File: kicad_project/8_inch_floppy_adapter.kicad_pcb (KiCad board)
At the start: 2 copper layers, 100 x 50 mm, 13 parts, among them J1 IDC02x17, J2 IDC02x17, J3 IDC02x25

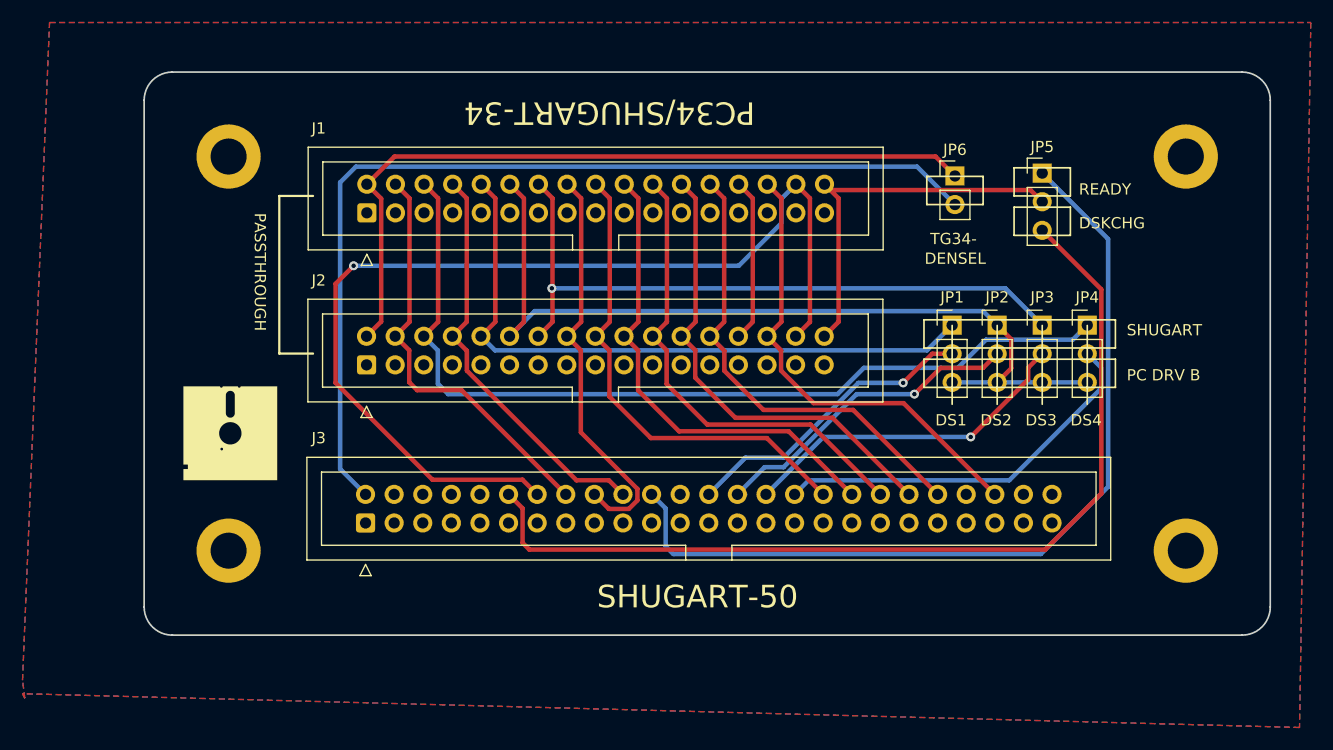
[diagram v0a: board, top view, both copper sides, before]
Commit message: Refine routing
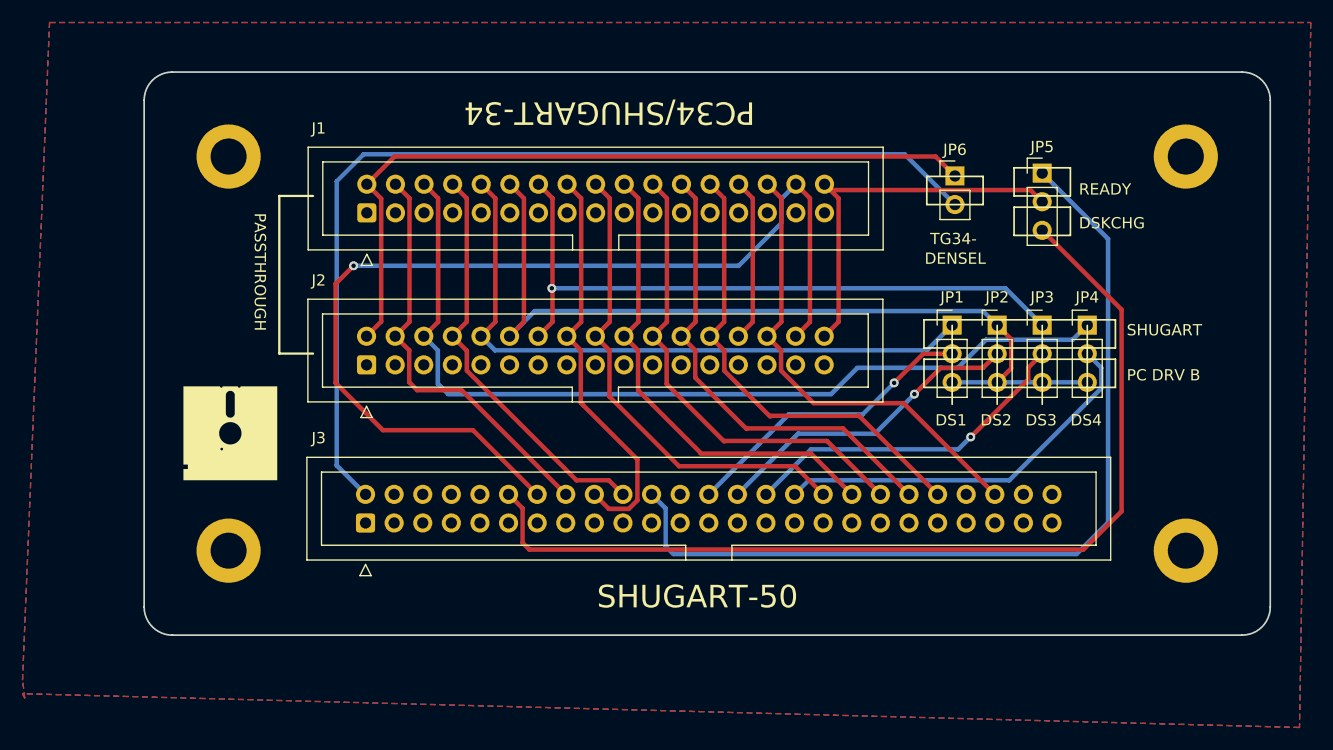
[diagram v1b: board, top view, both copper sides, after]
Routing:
- net 50_DSKCHG: track 84.1 -> 87.5 mm
- net 50_READY: track 77.5 -> 79.3 mm
- net 50_TG43: track 85.2 -> 86.6 mm

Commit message: Update makefile
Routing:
- net 50_READY: track 79.3 -> 83.9 mm
- net 34_RDY/DSKCHG: track 34.5 -> 37.8 mm
- net 50_DS4: track 34.7 -> 37.0 mm
- net 34_DS1/DRVSB: track 77.6 -> 79.7 mm
- net 34_DS2/DRVSA: track 59.5 -> 60.4 mm
